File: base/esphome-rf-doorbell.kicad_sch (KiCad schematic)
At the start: 59 parts, among them J1 B4B-XH, J2 CONUFL001-SMD-T, J3 Conn_01x01, J4 Conn_01x01, SW1 Boot, U1 MP5493GJ-Z, U2 RFM69W, U3 G3VM-31DR, U4 ESP32-S2-MINI-2, U5 G3VM-63ER, U6 TLP2391

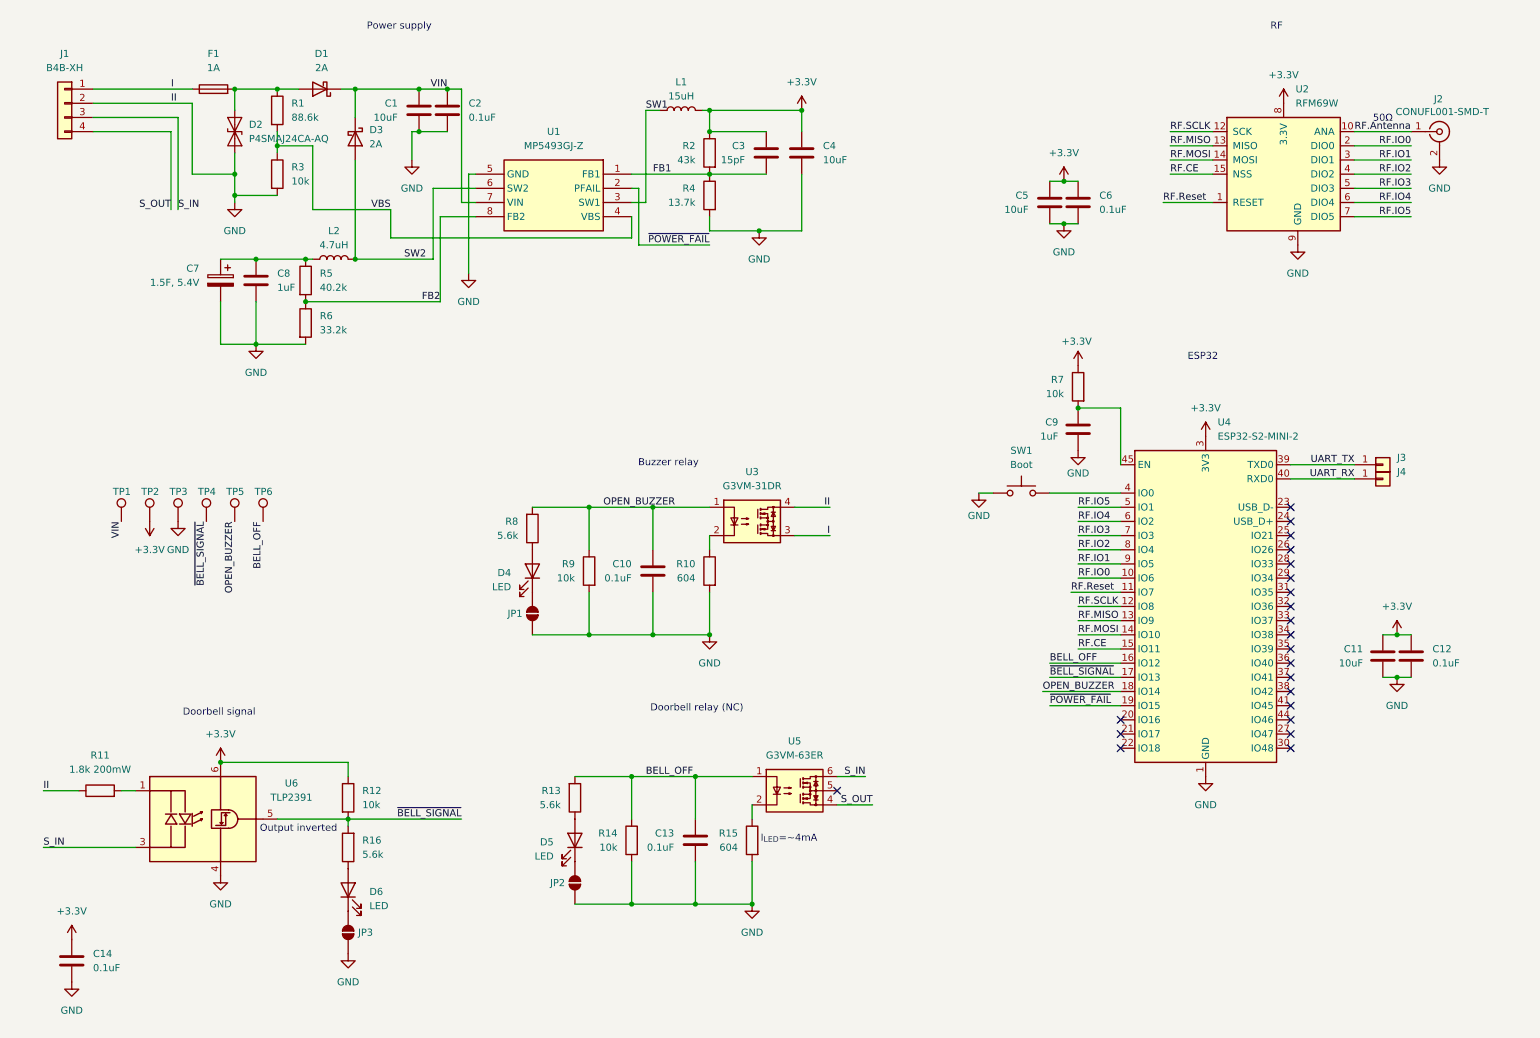
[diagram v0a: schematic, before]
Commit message: Add remote and firmware
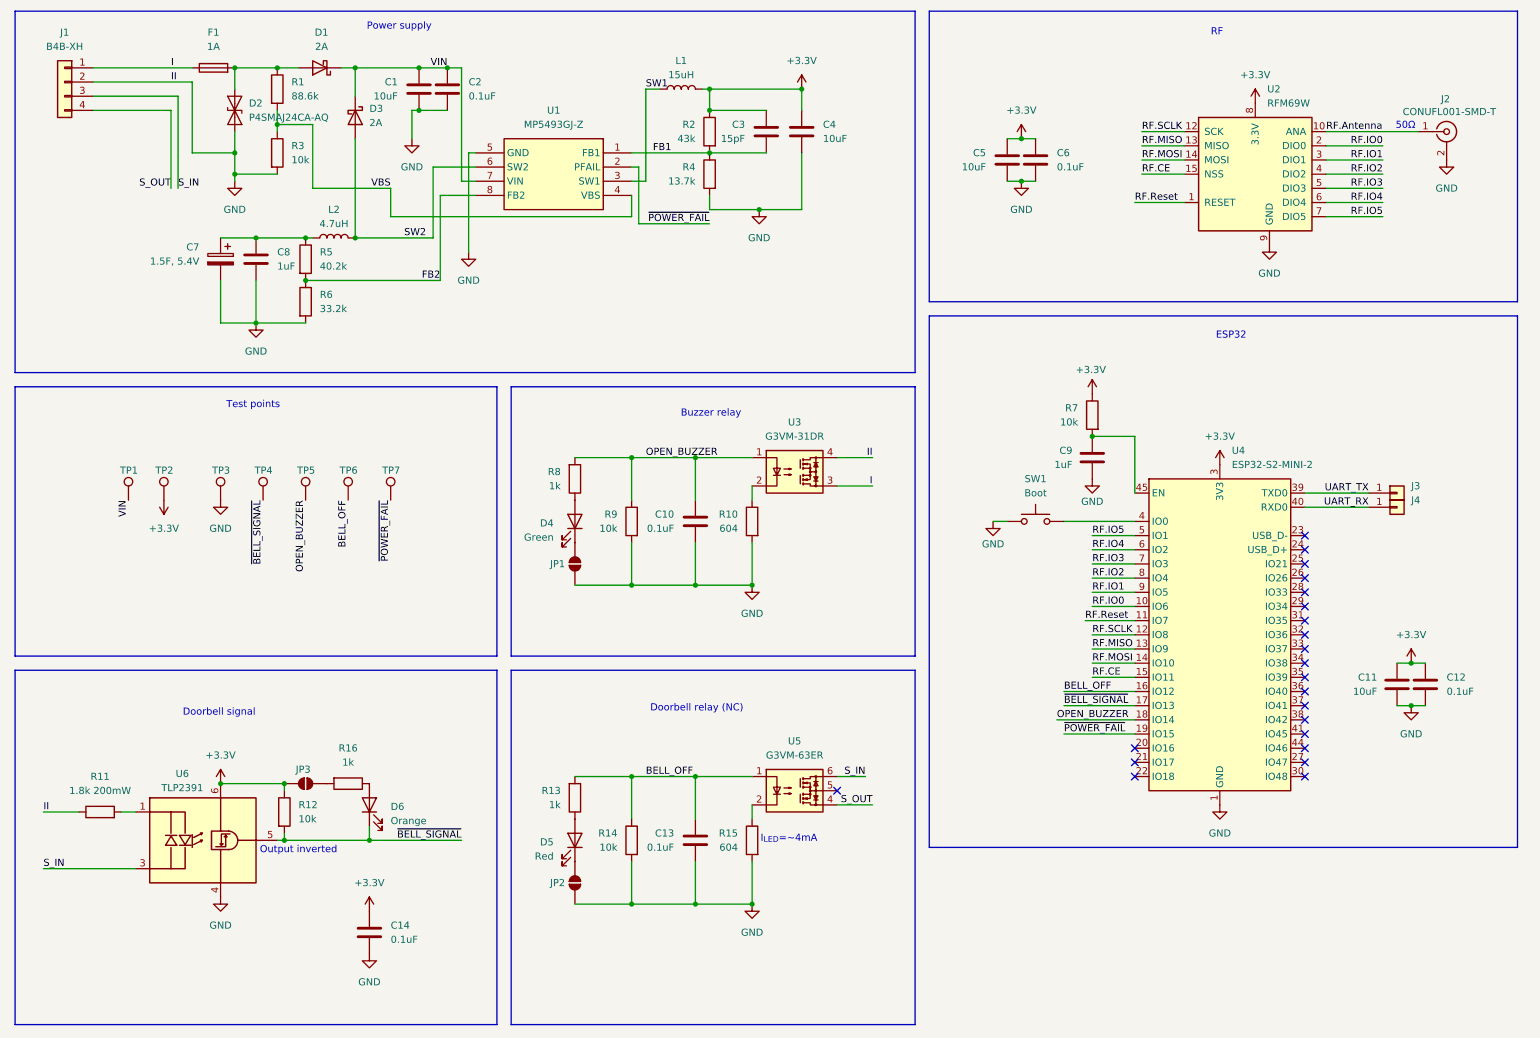
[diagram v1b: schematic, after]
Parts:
- added TP7: TestPoint, TestPoint:TestPoint_Pad_D1.5mm, symbol Connector:TestPoint
- C8: footprint Resistor_SMD:R_0603_1608Metric -> Capacitor_SMD:C_0603_1608Metric
- D4: value LED -> Green
- D5: value LED -> Red
- D6: value LED -> Orange
- JP1, JP2, JP3: footprint Jumper:SolderJumper-2_P1.3mm_Bridged_RoundedPad1.0x1.5mm -> Jumper:SolderJumper-2_P1.3mm_Open_RoundedPad1.0x1.5mm
- L2: footprint Inductor_SMD:L_APV_APH1040 -> Inductor_SMD:L_Coilcraft_XAL6060-XXX; MPN HPI1040-150 -> XAL6060-472MEC
- R13, R16, R8: value 5.6k -> 1k
- TP2, TP3: footprint TestPoint:TestPoint_Pad_D1.5mm -> TestPoint:TestPoint_Keystone_5000-5004_Miniature
- U3: footprint Package_DIP:SMDIP-4_W7.62mm -> lib:G3VM-21DR
- U5: footprint Package_DIP:SMDIP-6_W7.62mm -> lib:G3VM-21ER
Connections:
- net +3.3V: now also JP3.2 (B)
- net GND: no longer JP3.1 (A)
- net ~{BELL_SIGNAL}: now also D6.1 (K); no longer R16.2
- net ~{POWER_FAIL}: now also TP7.1
- new net: JP3.1 (A), R16.2
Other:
- note added: "Test points"
- title: (none) -> Smart STR HT2001 doorbell for integration with Homeassistant
- moved on the sheet: C1, C10, C11, C12, C14, C2, C3, C4, C5, C6, C7, C8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

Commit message: New board rev, frist draft of ESPHome component
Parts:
- removed C1: 10uF, Capacitor_SMD:C_0805_2012Metric, symbol Device:C
- removed C2: 0.1uF, Capacitor_SMD:C_0402_1005Metric, symbol Device:C
- removed C3: 15pF, Resistor_SMD:R_0402_1005Metric, symbol Device:C
- removed C4: 10uF, Capacitor_SMD:C_0603_1608Metric, symbol Device:C
- removed C7: 1.5F, 5.4V, lib:PHV5R4V155R, symbol Device:C_Polarized
- removed C8: 1uF, Capacitor_SMD:C_0603_1608Metric, symbol Device:C
- removed D1, D3: 2A, Diode_SMD:D_SMA, symbol Device:D_Schottky
- removed D2: P4SMAJ24CA-AQ, Diode_SMD:D_SMA, symbol Diode:SMAJ24CA
- removed F1: 1A, Fuse:Fuse_0603_1608Metric, symbol Device:Fuse
- removed L1: 15uH, Inductor_SMD:L_APV_ANR8040, symbol Device:L
- removed L2: 4.7uH, Inductor_SMD:L_Coilcraft_XAL6060-XXX, symbol Device:L
- removed R1: 88.6k, Resistor_SMD:R_0603_1608Metric, symbol Device:R
- removed R11: 1.8k 200mW, Resistor_SMD:R_0603_1608Metric, symbol Device:R
- removed R2: 43k, Resistor_SMD:R_0603_1608Metric, symbol Device:R
- removed R3: 10k, Resistor_SMD:R_0603_1608Metric, symbol Device:R
- removed R4: 13.7k, Resistor_SMD:R_0603_1608Metric, symbol Device:R
- removed R5: 40.2k, Resistor_SMD:R_0402_1005Metric, symbol Device:R
- removed R6: 33.2k, Resistor_SMD:R_0603_1608Metric, symbol Device:R
- removed TP7: TestPoint, TestPoint:TestPoint_Pad_D1.5mm, symbol Connector:TestPoint
- removed U1: MP5493GJ-Z, lib:SOT65P280X100-8N, symbol MP5493GJ-Z:MP5493GJ-Z
- added BT1: ~, Connector_Molex:Molex_PicoBlade_53261-0271_1x02-1MP_P1.25mm_Horizontal, symbol Device:Battery_Cell
- added C1, C11, C12: 1uF, Capacitor_SMD:C_0402_1005Metric, symbol Device:C_Small
- added C10: 10uF 10V, Capacitor_SMD:C_0603_1608Metric, symbol Device:C_Small
- added C13: 0.1uF, Capacitor_SMD:C_0402_1005Metric, symbol Device:C_Small
- added C14: 22uF 6.3V, Capacitor_SMD:C_0603_1608Metric, symbol Device:C_Small
- added C15: 4.7uF, Capacitor_SMD:C_0603_1608Metric, symbol Device:C
- added C16, C2: 47nF, Capacitor_SMD:C_0402_1005Metric, symbol Device:C_Small
- added C23: 1uF 50V, Capacitor_SMD:C_0805_2012Metric, symbol Device:C_Small
- added C3: 22uF 16V, Capacitor_SMD:C_0805_2012Metric, symbol Device:C_Small
- added C4: 10uF 25V, Capacitor_SMD:C_0603_1608Metric, symbol Device:C_Small
- added C5: 0.1uF 25V, Capacitor_SMD:C_0402_1005Metric, symbol Device:C_Small
- added C6: 4.7uF, Capacitor_SMD:C_0603_1608Metric, symbol Device:C_Small
- added C9: 330nF, Capacitor_SMD:C_0402_1005Metric, symbol Device:C_Small
- added D1: PMEG2005EJ-QX, Diode_SMD:D_SOD-323F, symbol Device:D_Schottky_Small
- added D2: SMBJ15CA, Diode_SMD:D_SMB, symbol Diode:SMAJ15CA
- added D3: Red, LED_SMD:LED_0603_1608Metric, symbol Device:LED_Small
- added D4: Green, LED_SMD:LED_0603_1608Metric, symbol Device:LED_Small
- added F1: 250mA, Fuse:Fuse_1206_3216Metric, symbol Device:Polyfuse_Small
- added FID1, FID2, FID3: Fiducial, Fiducial:Fiducial_0.5mm_Mask1mm, symbol Mechanical:Fiducial
- added JP1, JP2: SolderJumper_2_Open, Jumper:SolderJumper-2_P1.3mm_Open_RoundedPad1.0x1.5mm, symbol Jumper:SolderJumper_2_Open
- added L1: 1.5uH, Inductor_SMD:L_Wuerth_MAPI-4020, symbol Device:L_Small
- added L2: 2.2uH, Inductor_SMD:L_1210_3225Metric, symbol Device:L_Small
- added R1, R2: 1k, Resistor_SMD:R_0603_1608Metric, symbol Device:R_Small
- added R10: 0, Resistor_SMD:R_0402_1005Metric, symbol Device:R_Small
- added R11: 137k, Resistor_SMD:R_0603_1608Metric, symbol Device:R_Small
- added R12: 25m, Resistor_SMD:R_Shunt_Vishay_WSK2512_6332Metric_T1.19mm, symbol Device:R_Shunt
- added R13, R19: 4.7k, Resistor_SMD:R_0402_1005Metric, symbol Device:R
- added R14, R18: 4.7k, Resistor_SMD:R_1206_3216Metric, symbol Device:R
- added R3: 1.2k, Resistor_SMD:R_0603_1608Metric, symbol Device:R_Small
- added R4: 5.23k, Resistor_SMD:R_0402_1005Metric, symbol Device:R_Small
- added R5: 4.99k, Resistor_SMD:R_0402_1005Metric, symbol Device:R_Small
- added R6: 30.1k, Resistor_SMD:R_0402_1005Metric, symbol Device:R_Small
- added R7: 10k, Resistor_SMD:R_0603_1608Metric, symbol Device:R
- added R9: 619k, Resistor_SMD:R_0603_1608Metric, symbol Device:R_Small
- added RV1: 10k, Potentiometer_SMD:Potentiometer_Bourns_TC33X_Vertical, symbol Device:R_Potentiometer_Small
- added RV2: 5k 0.25W, Potentiometer_SMD:Potentiometer_Bourns_3214W_Vertical, symbol Device:R_Potentiometer_Small
- added TH1: 10k, Resistor_THT:R_Axial_DIN0204_L3.6mm_D1.6mm_P5.08mm_Vertical, symbol Device:Thermistor_NTC
- added TP1, TP11, TP4, TP5: TestPoint, TestPoint:TestPoint_Pad_D1.5mm, symbol Connector:TestPoint
- added U1: BQ25628E, lib:WQFN-HR18__RYK_TEX, symbol BQ25628E:BQ25628ERYKR
- added U3: TPS7A2033, Package_SON:Texas_X2SON-4_1x1mm_P0.65mm, symbol Regulator_Linear:TPS7A20xxxDQN
- added U4: MAX17261xxTD, Package_DFN_QFN:TDFN-14-1EP_3x3mm_P0.4mm_EP1.78x2.35mm, symbol Battery_Management:MAX17261xxTD
- added U5: TPS629206DRLR, lib:SOT5X3-8_DRL_TEX, symbol TPS629206:TPS629206DRLR
- R17: renamed from R10; footprint Resistor_SMD:R_0402_1005Metric_Pad0.72x0.64mm_HandSolder -> Resistor_SMD:R_0402_1005Metric
- R24: renamed from R15; footprint Resistor_SMD:R_0402_1005Metric_Pad0.72x0.64mm_HandSolder -> Resistor_SMD:R_0402_1005Metric
- U2: MPN (none) -> RFM69W
- U6: renamed from U3; MPN (none) -> G3VM-31DR
- U7: renamed from U4; MPN (none) -> ESP32-S2-MINI-2
- renumbered C9 to C17, C10 to C18, C11 to C19, C12 to C20, C14 to C21, C13 to C22, C5 to C7, C6 to C8, D4 to D5, D5 to D7, JP1 to JP3, JP3 to JP4, JP2 to JP5, R8 to R15, R9 to R16, R16 to R20, R13 to R21, R12 to R22, R14 to R23, R7 to R8, TP6 to TP10, TP1 to TP6, TP3 to TP7, TP4 to TP8, TP5 to TP9, U5 to U8, U6 to U9
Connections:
- net GND: now also U9.1 (A), C1.2, C10.1, C11.2, C12.2, C14.2, C15.2, C3.2, C4.2, C5.2, C6.2, C9.1, D2.1 (A1), R10.2, R11.2, R12.1, R3.1, R5.1, R6.1, R7.2, TH1.2, TP5.1, U1.15 (GND), U3.2 (GND), U3.5 (Pad), U5.5 (GND)
- net I: now also F1.1
- net S_IN: now also C23.2; no longer U9.3 (K)
- net VIN: now also C1.1, D1.1 (K), U1.18 (VBUS)
- net SDA1: now reaches U7.20 (IO16)
- net SDA1: now also R18.2, U1.12 (SDA)
- net ~{INT}: now reaches U7.21 (IO17)
- net ~{INT}: now also U1.11 (~{INT})
- net ~{CE}: now reaches U7.22 (IO18)
- net ~{CE}: now also R7.1, U1.14 (~{CE})
- net RF_PWR_EN: now reaches U7.25 (IO21)
- net RF_PWR_EN: now also U3.3 (EN)
- net SCL2: now reaches U7.31 (IO35)
- net SCL2: now also R13.2, U4.14 (SCL)
- net SDA2: now reaches U7.32 (IO36)
- net SDA2: now also R14.2, U4.13 (SDA)
- net BAT_ALERT: now reaches U7.33 (IO37)
- net BAT_ALERT: now also U4.12 (ALRT)
- net +3.3V renamed +3.3VP
- net +3.3VP: now also C14.1, L2.2, R13.1, R14.1, R18.1, R19.1, R9.1, U5.3 (VOS); no longer C7.1, C8.1, U2.8 (3.3V)
- net ~{POWER_FAIL} renamed SCL1
- net SCL1: now also R19.2, U1.13 (SCL)
- new net: C6.1, U1.2 (REGN)
- new net: RV2.2, RV2.3, U9.3 (K)
- new net: JP1.1 (A), U1.10 (STAT)
- new net: C4.1, C5.1, U1.17 (PMID)
- new net: JP2.1 (A), U1.3 (~{PG})
- new net: C9.2, R3.2, RV1.1, TP1.1, U1.4 (ILIM)
- new net: R4.2, U1.5 (TS_BIAS)
- new net: D1.2 (A), D2.2 (A2), F1.2
- new net: C13.2, C16.2, R12.3, U4.15 (GND), U4.8 (GND), U4.9 (CSPL)
- new net: R12.2, U4.7 (CSN)
- new net: R10.1, U5.8 (MODE)
- new net: C23.1, RV2.1, TP11.1
- new net: R11.1, R9.2, U5.1 (FB/VSET)
- new net: L2.1, U5.4 (SW)
- new net: D4.2 (A), R2.2
- new net: R5.2, RV1.2, RV1.3
- new net: D3.1 (K), JP1.2 (B)
- new net: C16.1, U4.11 (REG)
- new net: D4.1 (K), JP2.2 (B)
- new net: D3.2 (A), R1.2
- new net +3.3VA: C12.1, C7.1, C8.1, U2.8 (3.3V), U3.1 (OUT)
- new net +BATT: BT1.1 (+), C10.2, C13.1, U1.8 (BAT), U4.6 (BATT)
- new net BAT-: BT1.2 (-), R12.4
- new net BTST: C2.2, U1.1 (BTST)
- new net SW: C2.1, L1.1, U1.16 (SW)
- new net TH: R4.1, R6.2, TH1.1, U1.6 (TS), U4.1 (TH)
- new net VBUS: C11.1, C15.1, C3.1, L1.2, R1.1, R2.1, TP4.1, U1.9 (SYS), U3.4 (IN), U5.6 (VIN), U5.7 (EN)
- no-connect marks 22 -> 19
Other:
- note added: "Auto Mode"
- note added: "Battery fuel gauge"
- note added: "DC/DC for ESP32 and SSRs/opto coupler"
- note added: "I^{2}C slave address: 0x6A"
- note added: "I^{2}C slave address: 0x6C"
- note added: "Power path, battery charger"
- note added: "RF LDO"
- note added: "Test points, fiducials"
- note removed: "Power supply"
- note removed: "Test points"
- moved on the sheet: C18, C19, C20, C21, C22, D5, D6, D7, JP3, JP4, JP5, R15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

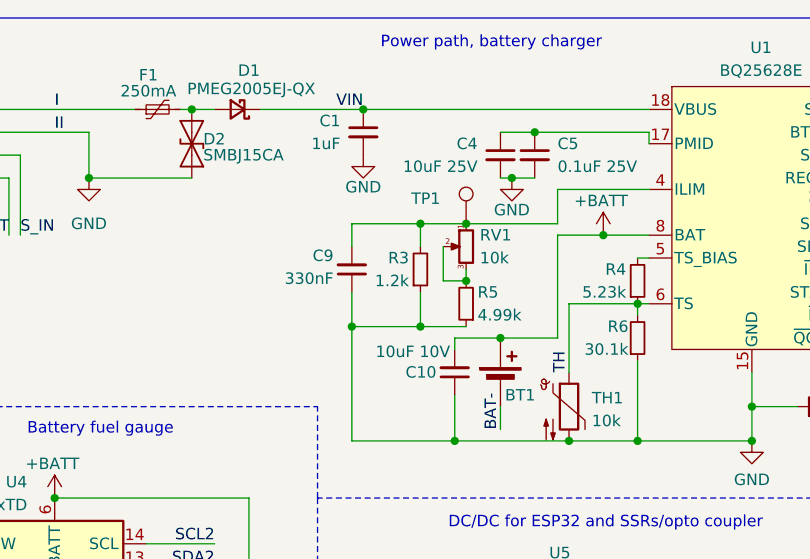
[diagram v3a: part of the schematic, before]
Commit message: Fix read_register_word_ call - use reference not pointer
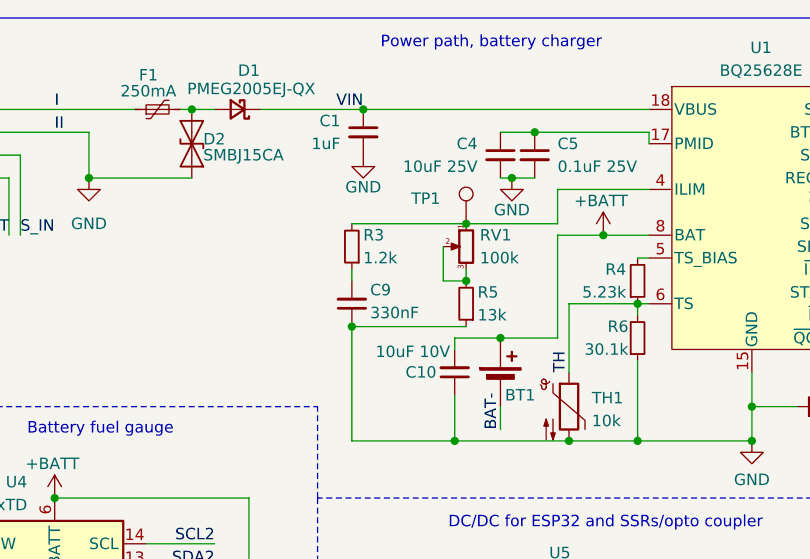
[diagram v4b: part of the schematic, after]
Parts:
- R5: value 4.99k -> 13k
- RV1: value 10k -> 100k; MPN TC33X-1-103E -> TC33X-2-104E
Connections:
- net GND: no longer R3.1
- net at R3.2, RV1.1, TP1.1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: no longer C9.2
- new net: C9.2, R3.1
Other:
- moved on the sheet: C9, R3
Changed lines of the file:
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@@
 	)
 	(junction
+		(at 67.31 48.26)
+		(diameter 0)
+		(color 0 0 0 0)
+	)
+	(junction
 		(at 25.4 92.71)
 		(diameter 0)
@@
 	)
 	(junction
-		(at 74.93 48.26)
-		(diameter 0)
-		(color 0 0 0 0)
-	)
-	(junction
 		(at 80.01 36.83)
 		(diameter 0)
@@
 	)
 	(junction
-		(at 74.93 36.83)
-		(diameter 0)
-		(color 0 0 0 0)
-	)
-	(junction
 		(at 34.29 67.31)
 		(diameter 0)
@@
 	)
 	(junction
-		(at 67.31 48.26)
-		(diameter 0)
-		(color 0 0 0 0)
-	)
-	(junction
 		(at 85.09 31.75)
 		(diameter 0)
@@
 	(wire
 		(pts
+			(xy 67.31 36.83) (xy 80.01 36.83)
+		)
+		(stroke
+			(width 0)
+			(type default)
+		)
+	)
+	(wire
+		(pts
 			(xy 15.24 168.91) (xy 29.21 168.91)
 		)
@@
 		)
 	)
-	(polyline
+	(wire
 		(pts
-			(xy 13.97 57.15) (xy 63.5 57.15)
+			(xy 67.31 48.26) (xy 80.01 48.26)
 		)
 		(stroke
 			(width 0)
-			(type dash)
+			(type default)
 		)
 	)
-	(wire
+	(polyline
 		(pts
-			(xy 67.31 48.26) (xy 74.93 48.26)
+			(xy 13.97 57.15) (xy 63.5 57.15)
 		)
 		(stroke
 			(width 0)
-			(type default)
+			(type dash)
 		)
 	)
@@
 	(wire
 		(pts
-			(xy 74.93 39.37) (xy 74.93 36.83)
-		)
-		(stroke
-			(width 0)
-			(type default)
-		)
-	)
-	(wire
-		(pts
 			(xy 214.63 90.17) (xy 214.63 100.33)
 		)
@@
 	(wire
 		(pts
-			(xy 67.31 36.83) (xy 74.93 36.83)
-		)
-		(stroke
-			(width 0)
-			(type default)
-		)
-	)
-	(wire
-		(pts
 			(xy 95.25 38.1) (xy 100.33 38.1)
 		)
@@
 	(wire
 		(pts
+			(xy 67.31 43.18) (xy 67.31 41.91)
+		)
+		(stroke
+			(width 0)
+			(type default)
+		)
+	)
+	(wire
+		(pts
 			(xy 83.82 26.67) (xy 87.63 26.67)
 		)
@@
 	(wire
 		(pts
-			(xy 80.01 36.83) (xy 74.93 36.83)
-		)
-		(stroke
-			(width 0)
-			(type default)
-		)
-	)
-	(wire
-		(pts
 			(xy 200.66 140.97) (xy 214.63 140.97)
 		)
@@
 	(wire
 		(pts
-			(xy 74.93 48.26) (xy 74.93 44.45)
-		)
-		(stroke
-			(width 0)
-			(type default)
-		)
-	)
-	(wire
-		(pts
 			(xy 111.76 57.15) (xy 111.76 53.34)
 		)
@@
 	(wire
 		(pts
-			(xy 67.31 39.37) (xy 67.31 36.83)
-		)
-		(stroke
-			(width 0)
-			(type default)
-		)
-	)
-	(wire
-		(pts
 			(xy 106.68 82.55) (xy 106.68 80.01)
 		)
@@
 	(wire
 		(pts
-			(xy 74.93 48.26) (xy 80.01 48.26)
-		)
-		(stroke
-			(width 0)
-			(type default)
-		)
-	)
-	(wire
-		(pts
 			(xy 148.59 170.18) (xy 148.59 172.72)
 		)
@@
 	(wire
 		(pts
-			(xy 67.31 44.45) (xy 67.31 48.26)
-		)
-		(stroke
-			(width 0)
-			(type default)
-		)
-	)
-	(wire
-		(pts
 			(xy 138.43 165.1) (xy 148.59 165.1)
 		)
@@
 	(symbol
 		(lib_id "Device:R_Small")
-		(at 74.93 41.91 0)
-		(mirror x)
+		(at 67.31 39.37 180)
 		(unit 1)
 		(exclude_from_sim no)
@@
 		(dnp no)
 		(property "Reference" "R3"
-			(at 73.66 40.64 0)
+			(at 68.58 38.1 0)
 			(effects
 				(font
@@
 		)
 		(property "Value" "1.2k"
-			(at 73.66 43.18 0)
+			(at 68.58 40.64 0)
 			(effects
 				(font
@@
 		)
 		(property "Footprint" "Resistor_SMD:R_0603_1608Metric"
-			(at 74.93 41.91 0)
+			(at 67.31 39.37 0)
 			(effects
 				(font
@@
 		)
 		(property "Datasheet" "~"
-			(at 74.93 41.91 0)
+			(at 67.31 39.37 0)
 			(effects
 				(font
@@
 		)
 		(property "Description" "Resistor, small symbol"
-			(at 74.93 41.91 0)
+			(at 67.31 39.37 0)
 			(effects
 				(font
@@
 			)
 		)
-		(property "Value" "10k"
+		(property "Value" "100k"
 			(at 81.534 40.64 0)
 			(effects
@@
 			)
 		)
-		(property "MPN" "TC33X-1-103E"
+		(property "MPN" "TC33X-2-104E"
 			(at 80.01 39.37 0)
 			(effects
@@
 	(symbol
 		(lib_id "Device:C_Small")
-		(at 67.31 41.91 0)
-		(mirror x)
+		(at 67.31 45.72 180)
 		(unit 1)
 		(exclude_from_sim no)
@@
 		(dnp no)
 		(property "Reference" "C9"
-			(at 65.278 40.386 0)
+			(at 69.342 44.196 0)
 			(effects
 				(font
@@
 		)
 		(property "Value" "330nF"
-			(at 65.278 42.926 0)
+			(at 69.342 46.736 0)
 			(effects
 				(font
@@
 		)
 		(property "Footprint" "Capacitor_SMD:C_0402_1005Metric"
-			(at 67.31 41.91 0)
+			(at 67.31 45.72 0)
 			(effects
 				(font
@@
 		)
 		(property "Datasheet" "~"
-			(at 67.31 41.91 0)
+			(at 67.31 45.72 0)
 			(effects
 				(font
@@
 		)
 		(property "Description" "Unpolarized capacitor, small symbol"
-			(at 67.31 41.91 0)
+			(at 67.31 45.72 0)
 			(effects
 				(font
@@
 		)
 		(instances
-			(project ""
+			(project "esphome-rf-doorbell"
 				(path "/b07d5988-2788-4b3b-a250-602b43e32b02"
 					(reference "C9")
@@
 			)
 		)
-		(property "Value" "4.99k"
+		(property "Value" "13k"
 			(at 81.28 46.99 0)
 			(effects

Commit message: Update interrupt pin mapping
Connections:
- net BAT_ALERT: now also U7.25 (IO21); no longer U7.33 (IO37)
- net RF_PWR_EN: now also U7.28 (IO33); no longer U7.25 (IO21)

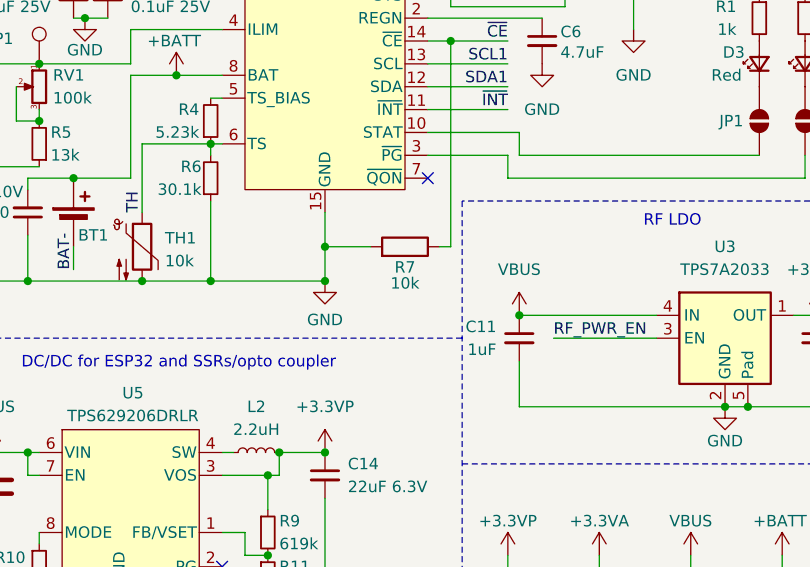
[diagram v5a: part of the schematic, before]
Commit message: Update schematics with latest findings
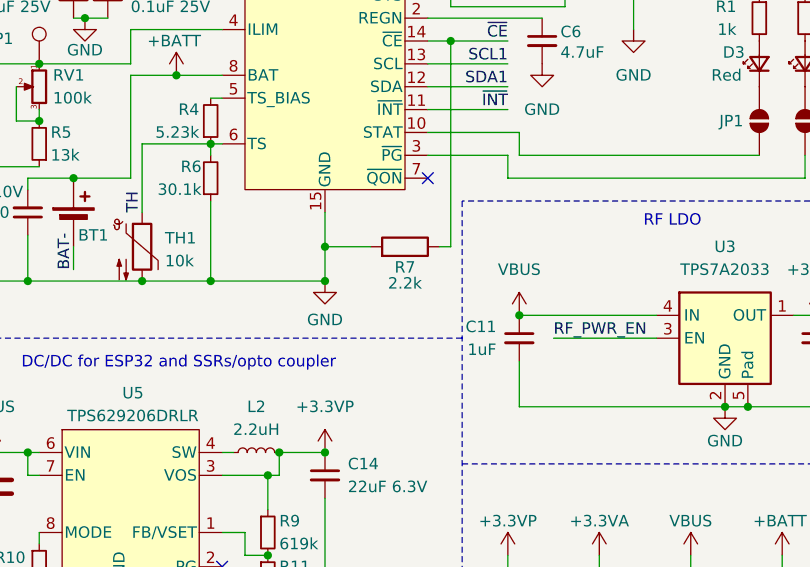
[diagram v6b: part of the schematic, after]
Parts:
- R7: value 10k -> 2.2k
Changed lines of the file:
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@@
 			)
 		)
-		(property "Datasheet" "~"
+		(property "Datasheet" "https://www.yageogroup.com/content/datasheet/asset/file/SMD1206_1"
 			(at 45.72 24.13 0)
 			(effects
@@
 			)
 		)
-		(property "Value" "10k"
+		(property "Value" "2.2k"
 			(at 120.65 61.214 90)
 			(effects
